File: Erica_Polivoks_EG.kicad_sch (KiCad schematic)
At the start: 99 parts, among them J1 GATE IN, J2 INV EG OUT, J3 Eurorack_Power_10pin_Unshroud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, J4 GATE IN, J5 GATE IN, Q1 2N3904, Q2 2N3904, Q3 2N3904, Q4 2N3904, Q5 2N3904, Q6 2N3904, Q7 2N3906, Q8 2N3906, Q9 2N3906, SW1 SW_SPDT, SW2 SW_SPDT, U1 TL074

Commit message: passed ERC
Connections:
- net TP1: no longer names the net of R10.2, R7.2, U1.1
- net TP10: no longer names the net of C7.1, RV1.1, RV1.2, RV2.1, RV2.2, RV3.1, RV3.2, U1.13 (-)
- net TP2: no longer names the net of Q5.3 (C), R3.2
- net TP3: no longer names the net of R14.2, R23.1, R24.1, RV4.1, U1.6 (-)
- net TP4: no longer names the net of D4.2 (A), D5.2 (A), Q7.3 (C), R15.2, R19.1, R20.1, R21.2
- net TP5: no longer names the net of D3.2 (A), D5.1 (K), U1.5 (+)
- net TP7: no longer names the net of Q6.2 (B), R25.2, SW2.2 (B)

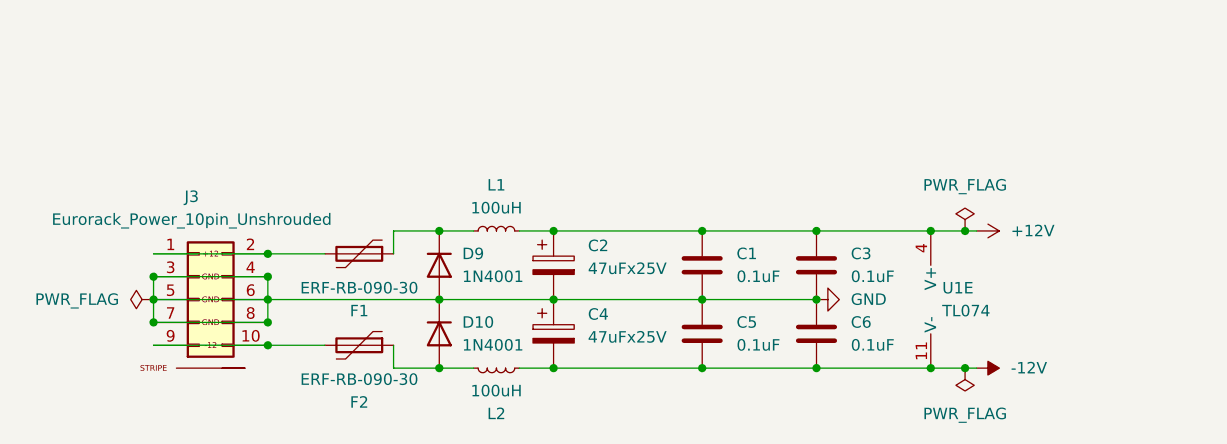
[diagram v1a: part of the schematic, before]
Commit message: removed polyfuses, polarity protection diodes and inductors from power section of schematic
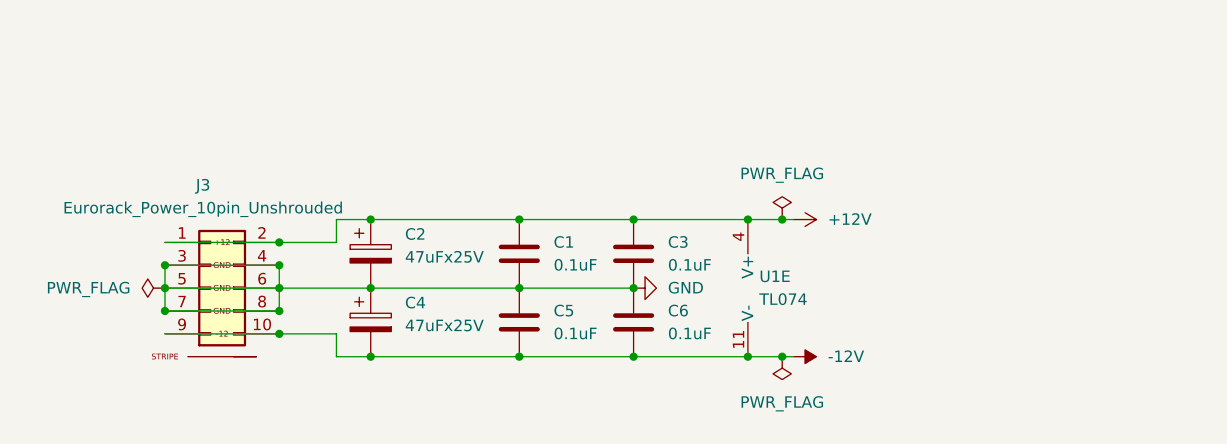
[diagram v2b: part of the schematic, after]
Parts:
- removed D10, D9: 1N4001, Diode_THT:D_DO-41_SOD81_P10.16mm_Horizontal, symbol Diode:1N4001
- removed F1, F2: ERF-RB-090-30, symbol Device:Polyfuse
- removed L1, L2: 100uH, symbol Device:L_Small
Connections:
- net +12V: now also J3.1 (+12V), J3.2 (+12V)
- net -12V: now also J3.10 (-12V), J3.9 (-12V)
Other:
- moved on the sheet: C1, C2, C3, C4, C5, C6, J3, U1E

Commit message: schematic double checked
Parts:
- removed SW1, SW2: SW_SPDT, symbol Switch:SW_SPDT
- added SW1: SW_DPDT_x2, symbol Switch:SW_DPDT_x2
- J4: value GATE IN -> GATE DELAY OUT
- J5: value GATE IN -> EG OUT
- R25: value 10M -> 1M
- R34: value NU -> NU 39K
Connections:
- net +12V: now also R5.1; no longer Q3.3 (C), Q8.3 (C), R1.2, R2.2, R5.2
- net -12V: now also SW1.3 (C)
- net GND: now also SW1.6 (C)
- net at R20.2, R27.1, R28.1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: now also U1.1; no longer U1.7
- net at D1.1 (K), D2.2 (A), R4.2: now also U1.13 (-); no longer U1.3 (+)
- net at Q6.2 (B), R25.2: now also SW1.5 (B)
- net at R35.2, R36.1: now also U1.9 (-); no longer U1.10 (+)
- net at R33.1, R34.1: now also U1.10 (+); no longer U1.9 (-)
- net at D12.1 (K), D13.2 (A), R39.2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: no longer D6.1 (K), Q3.2 (B), R16.2, R27.2, R28.2
- net at R7.1, R8.2, R9.2: now also U1.12 (+); no longer U1.2 (-)
- net at R10.2, R7.2: now also U1.14; no longer U1.1
- net at D14.1 (K), D15.2 (A), R32.1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: now also U1.7; no longer U1.14
- net at C7.1, RV1.1, RV1.2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: now also U1.5 (+); no longer U1.13 (-)
- net at R14.2, R23.1, RV4.1: now also U1.2 (-); no longer R24.1, U1.6 (-)
- net at RV4.2: now also SW1.4 (A)
- net at J1.1 (SIG), R4.1, R6.2: no longer R5.1
- net at R45.1, R49.2, R50.1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: now also U1.6 (-); no longer U1.12 (+)
- net at J1.3 (SW): now also R5.2
- net at R19.2: now also SW1.2 (B)
- net at D3.2 (A), D5.1 (K): now also R24.1, U1.3 (+); no longer U1.5 (+)
- new net: Q8.3 (C), R1.2
- new net: R16.2, R28.2
- new net: D6.1 (K), Q3.2 (B), R27.2
- new net: Q3.3 (C), R2.2
- no-connect marks 5 -> 4
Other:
- moved on the sheet: D1, D2, D5, D6, J1, Q5, R15, R21, R22, R24, R4, R41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

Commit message: pcb routed
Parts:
- C1, C3, C5, C6: footprint (none) -> Capacitor_THT:C_Axial_L3.8mm_D2.6mm_P7.50mm_Horizontal
- C2, C4, C7: footprint (none) -> Capacitor_THT:CP_Radial_D5.0mm_P2.50mm
- D11, D18: footprint (none) -> PCM_4ms_LED:LED_3mm_C1A2
- J1, J2, J4, J5: footprint 4ms_Jack:EighthInch_PJ398SM -> Library:EighthInch_PJ398SM_3mmNPTH
- J3: footprint 4ms_Connector:Pins_2x05_2.54mm_TH_Europower -> Library:IDC-Header_2x05_P2.54mm_Vertical_Euro_Power_Striped
- R1, R10, R11, R12, R13, R14, R15, R16, R17, R18, R19, R2, R20, R21, R22, R23, R24, R25, R26, R27, R28, R29, R3, R30, R31, R32, R33, R34, R35, R36, R37, R38, R39, R4, R40, R41, R42, R43, R44, R45, R46, R47, R48, R49, R5, R50, R51, R6, R7, R8, R9: footprint (none) -> Resistor_THT:R_Axial_DIN0207_L6.3mm_D2.5mm_P7.62mm_Horizontal
- RV1, RV2, RV3, RV4: footprint (none) -> Library:Pot_9mm_DShaft_RemovedPins4_5
- SW1: footprint (none) -> PCM_4ms_Switch:Switch_Toggle_DPDT_SubMini
- U1: footprint (none) -> Package_DIP:DIP-14_W7.62mm_Socket

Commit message: v1.0 ready for production
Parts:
- D11: value GATE DELAY (YELLOW LED) -> GATE DELAY LED
- D18: value EG OUT (YELLOW LED) -> EG OUT LED
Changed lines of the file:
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@@
 			)
 		)
-		(property "Value" "EG OUT (YELLOW LED)"
+		(property "Value" "EG OUT LED"
 			(at 276.86 79.0575 0)
 			(effects
@@
 			)
 		)
-		(property "Value" "GATE DELAY (YELLOW LED)"
+		(property "Value" "GATE DELAY LED"
 			(at 242.8875 20.32 0)
 			(effects

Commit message: v1.0 ready for production
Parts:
- C1, C3, C5, C6: Silkscreen Value (none) -> 104
- C2, C4: Silkscreen Value (none) -> ◀47uF
- C7: Silkscreen Value (none) -> 4.7uF
- D1, D12, D13, D14, D15, D2, D3, D4, D5, D6, D7, D8: footprint Diode_THT:D_DO-35_SOD27_P7.62mm_Horizontal -> Library:D_DO-35_SOD27_P7.62mm_Horizontal_Widened_No_K; Silkscreen Value (none) -> 4148
- D11: value GATE DELAY LED -> LED
- D18: value EG OUT LED -> LED
- J4: Silkscreen Value (none) -> G. DELAY OUT
- Q1, Q2, Q3, Q4, Q5, Q6: Silkscreen Value (none) -> 4▼
- Q7, Q8, Q9: Silkscreen Value (none) -> 6▼
- R37, R44: Silkscreen Value (none) -> ◀470
- R47: Silkscreen Value (none) -> ▲100k
- R5: Silkscreen Value (none) -> ◀100k
- RV1: value 1M LOG "ATTACK" -> 1M LOG
- RV2: value 1M LOG "DECAY" -> 1M LOG
- RV3: value 1M LOG "RELEASE" -> 1M LOG
- RV4: value 100k LOG "SUSTAIN" -> 100k LOG
- SW1: footprint PCM_4ms_Switch:Switch_Toggle_DPDT_SubMini -> Library:Switch_Toggle_DPDT_MS202; Silkscreen Value (none) -> MS-202

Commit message: v1.0 ready for production - added actual HP-size outli]ne on User.Dawings layer
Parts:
- C7: Silkscreen Value 4.7uF -> ◀4.7uF
- J3: footprint Library:IDC-Header_2x05_P2.54mm_Vertical_Euro_Power_Striped -> Library:IDC-Header_2x05_P2.54mm_Vertical_Euro_Power_Striped_ThickerText
- Q1: Silkscreen Value 4▼ -> 4▲
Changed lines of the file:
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@@
 			)
 		)
-		(property "Footprint" "Library:IDC-Header_2x05_P2.54mm_Vertical_Euro_Power_Striped"
+		(property "Footprint" "Library:IDC-Header_2x05_P2.54mm_Vertical_Euro_Power_Striped_ThickerText"
 			(at 39.37 190.5 0)
 			(effects
@@
 			)
 		)
-		(property "Silkscreen Value" "4.7uF"
+		(property "Silkscreen Value" "◀4.7uF"
 			(at 194.31 123.19 0)
 			(effects
@@
 			)
 		)
-		(property "Silkscreen Value" "4▼"
+		(property "Silkscreen Value" "4▲"
 			(at 269.24 93.98 0)
 			(effects

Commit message: most of V1.1 changes completed
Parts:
- C1, C3: footprint Capacitor_THT:C_Axial_L3.8mm_D2.6mm_P7.50mm_Horizontal -> Capacitor_THT:C_Disc_D3.0mm_W1.6mm_P2.50mm; Silkscreen Value 104 -> 104▶
- C5, C6: footprint Capacitor_THT:C_Axial_L3.8mm_D2.6mm_P7.50mm_Horizontal -> Capacitor_THT:C_Disc_D3.0mm_W1.6mm_P2.50mm; Silkscreen Value 104 -> ◀104
- Q1, Q2, Q3, Q4, Q5, Q6, Q7, Q8, Q9: footprint Package_TO_SOT_THT:TO-92_Inline -> Library:TO-92L_Inline_Wider
- R34: value NU 39K -> NU 39K
- RV1, RV2, RV3: value 1M LOG -> 1M A
- RV4: value 100k LOG -> 100k A
- U1: Silkscreen (none) -> TL074; Silkscreen Value (none) -> TL074▶
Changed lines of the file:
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@@
 			)
 		)
-		(property "Description" "SW_DPDT "
+		(property "Description" "SW_DPDT"
 			(at 148.59 62.23 0)
 			(effects
@@
 			)
 		)
-		(property "Footprint" "Capacitor_THT:C_Axial_L3.8mm_D2.6mm_P7.50mm_Horizontal"
+		(property "Footprint" "Capacitor_THT:C_Disc_D3.0mm_W1.6mm_P2.50mm"
 			(at 70.8152 180.34 0)
 			(effects
@@
 			)
 		)
-		(property "Silkscreen Value" "104"
+		(property "Silkscreen Value" "104▶"
 			(at 69.85 176.53 0)
 			(effects
@@
 			)
 		)
+		(property "Silkscreen" "TL074"
+			(at 238.76 140.97 0)
+			(effects
+				(font
+					(size 1.27 1.27)
+				)
+				(hide yes)
+			)
+		)
+		(property "Silkscreen Value" "TL074▶"
+			(at 238.76 140.97 0)
+			(effects
+				(font
+					(size 1.27 1.27)
+				)
+				(hide yes)
+			)
+		)
 		(pin "5"
 		)
@@
 			)
 		)
+		(property "Silkscreen" "TL074"
+			(at 143.51 88.9 0)
+			(effects
+				(font
+					(size 1.27 1.27)
+				)
+				(hide yes)
+			)
+		)
+		(property "Silkscreen Value" "TL074▶"
+			(at 143.51 88.9 0)
+			(effects
+				(font
+					(size 1.27 1.27)
+				)
+				(hide yes)
+			)
+		)
 		(pin "5"
 		)
@@
 			)
 		)
+		(property "Silkscreen" "TL074"
+			(at 66.04 83.82 0)
+			(effects
+				(font
+					(size 1.27 1.27)
+				)
+				(hide yes)
+			)
+		)
+		(property "Silkscreen Value" "TL074▶"
+			(at 66.04 83.82 0)
+			(effects
+				(font
+					(size 1.27 1.27)
+				)
+				(hide yes)
+			)
+		)
 		(pin "5"
 		)
@@
 			)
 		)
-		(property "Footprint" "Package_TO_SOT_THT:TO-92_Inline"
+		(property "Footprint" "Library:TO-92L_Inline_Wider"
 			(at 102.87 61.595 0)
 			(effects
@@
 			)
 		)
+		(property "Silkscreen" "TL074"
+			(at 229.87 115.57 0)
+			(effects
+				(font
+					(size 1.27 1.27)
+				)
+				(hide yes)
+			)
+		)
+		(property "Silkscreen Value" "TL074▶"
+			(at 229.87 115.57 0)
+			(effects
+				(font
+					(size 1.27 1.27)
+				)
+				(hide yes)
+			)
+		)
 		(pin "5"
 		)
@@
 			)
 		)
-		(property "Footprint" "Package_TO_SOT_THT:TO-92_Inline"
+		(property "Footprint" "Library:TO-92L_Inline_Wider"
 			(at 274.32 95.885 0)
 			(effects
@@
 			)
 		)
-		(property "Footprint" "Package_TO_SOT_THT:TO-92_Inline"
+		(property "Footprint" "Library:TO-92L_Inline_Wider"
 			(at 191.77 104.775 0)
 			(effects
@@
 			)
 		)
-		(property "Footprint" "Package_TO_SOT_THT:TO-92_Inline"
+		(property "Footprint" "Library:TO-92L_Inline_Wider"
 			(at 243.84 32.385 0)
 			(effects
@@
 			)
 		)
-		(property "Footprint" "Capacitor_THT:C_Axial_L3.8mm_D2.6mm_P7.50mm_Horizontal"
+		(property "Footprint" "Capacitor_THT:C_Disc_D3.0mm_W1.6mm_P2.50mm"
 			(at 83.5152 187.96 0)
 			(effects
@@
 			)
 		)
-		(property "Silkscreen Value" "104"
+		(property "Silkscreen Value" "◀104"
 			(at 82.55 184.15 0)
 			(effects
@@
 			)
 		)
-		(property "Footprint" "Capacitor_THT:C_Axial_L3.8mm_D2.6mm_P7.50mm_Horizontal"
+		(property "Footprint" "Capacitor_THT:C_Disc_D3.0mm_W1.6mm_P2.50mm"
 			(at 70.8152 187.96 0)
 			(effects
@@
 			)
 		)
-		(property "Silkscreen Value" "104"
+		(property "Silkscreen Value" "◀104"
 			(at 69.85 184.15 0)
 			(effects
@@
 			)
 		)
-		(property "Value" "1M LOG"
+		(property "Value" "1M A"
 			(at 29.21 44.45 90)
 			(effects
@@
 			)
 		)
-		(property "Description" " DECAY"
+		(property "Description" "DECAY"
 			(at 36.068 44.45 90)
 			(effects
@@
 			)
 		)
-		(property "Footprint" "Package_TO_SOT_THT:TO-92_Inline"
+		(property "Footprint" "Library:TO-92L_Inline_Wider"
 			(at 170.815 104.14 0)
 			(effects
@@
 			)
 		)
+		(property "Silkscreen" "TL074"
+			(at 97.79 180.34 0)
+			(effects
+				(font
+					(size 1.27 1.27)
+				)
+				(hide yes)
+			)
+		)
+		(property "Silkscreen Value" "TL074▶"
+			(at 97.79 180.34 0)
+			(effects
+				(font
+					(size 1.27 1.27)
+				)
+				(hide yes)
+			)
+		)
 		(pin "5"
 		)
@@
 			)
 		)
-		(property "Value" "100k LOG"
+		(property "Value" "100k A"
 			(at 121.92 113.0299 0)
 			(effects
@@
 			)
 		)
-		(property "Description" " SUSTAIN"
+		(property "Description" "SUSTAIN"
 			(at 117.602 115.824 0)
 			(effects
@@
 			)
 		)
-		(property "Footprint" "Capacitor_THT:C_Axial_L3.8mm_D2.6mm_P7.50mm_Horizontal"
+		(property "Footprint" "Capacitor_THT:C_Disc_D3.0mm_W1.6mm_P2.50mm"
 			(at 83.5152 180.34 0)
 			(effects
@@
 			)
 		)
-		(property "Silkscreen Value" "104"
+		(property "Silkscreen Value" "104▶"
 			(at 82.55 176.53 0)
 			(effects
@@
 			)
 		)
-		(property "Footprint" "Package_TO_SOT_THT:TO-92_Inline"
+		(property "Footprint" "Library:TO-92L_Inline_Wider"
 			(at 92.71 94.615 0)
 			(effects
@@
 			)
 		)
-		(property "Footprint" "Package_TO_SOT_THT:TO-92_Inline"
+		(property "Footprint" "Library:TO-92L_Inline_Wider"
 			(at 82.55 120.015 0)
 			(effects
@@
 			)
 		)
-		(property "Value" "1M LOG"
+		(property "Value" "1M A"
 			(at 29.21 31.75 90)
 			(effects
@@
 			)
 		)
-		(property "Value" "1M LOG"
+		(property "Value" "1M A"
 			(at 29.21 57.15 90)
 			(effects
@@
 			)
 		)
-		(property "Description" " RELEASE"
+		(property "Description" "RELEASE"
 			(at 37.084 57.15 90)
 			(effects
@@
 			)
 		)
-		(property "Footprint" "Package_TO_SOT_THT:TO-92_Inline"
+		(property "Footprint" "Library:TO-92L_Inline_Wider"
 			(at 191.77 90.805 0)
 			(effects
@@
 			)
 		)
-		(property "Value" " NU 39K"
+		(property "Value" "NU 39K"
 			(at 234.95 149.86 90)
 			(effects
@@
 			)
 		)
-		(property "Footprint" "Package_TO_SOT_THT:TO-92_Inline"
+		(property "Footprint" "Library:TO-92L_Inline_Wider"
 			(at 191.77 57.785 0)
 			(effects
@@
 			)
 		)
-		(property "Description" "SW_DPDT "
+		(property "Description" "SW_DPDT"
 			(at 148.59 114.3 0)
 			(effects
